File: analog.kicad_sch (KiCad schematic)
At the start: 0 parts

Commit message: Add analog schematic and refine wiring on top.
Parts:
- added C16: 100nF, Capacitor_SMD:C_0603_1608Metric_Pad1.08x0.95mm_HandSolder, symbol Device:C
- added D1, D2: BZT52H-AD3V3-QX, Diode_SMD:D_SOD-123F, symbol Diode:BZT52Bxx
- added R29: 0R, Resistor_SMD:R_0603_1608Metric_Pad0.98x0.95mm_HandSolder, symbol Device:R
- added R30: 15K, Resistor_SMD:R_0603_1608Metric_Pad0.98x0.95mm_HandSolder, symbol Device:R
- added R31: 10K, Resistor_SMD:R_0603_1608Metric_Pad0.98x0.95mm_HandSolder, symbol Device:R
- added R32: 4.7K, Resistor_SMD:R_0603_1608Metric_Pad0.98x0.95mm_HandSolder, symbol Device:R
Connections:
- new net: D1.1 (K), R29.1, R30.2, R31.2
- new net GNDA: C16.1, D1.2 (A), D2.2 (A), R30.1
- new net Van: R32.2
- new net moistv_mcu: C16.2, R31.1
- new net moistv_sensor: R29.2
- new net onewire_mcu: D2.1 (K), R32.1
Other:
- note added: "fc=0.1592KHz"

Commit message: Add protected Vbat charger input.
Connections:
- net GNDA renamed GNDD

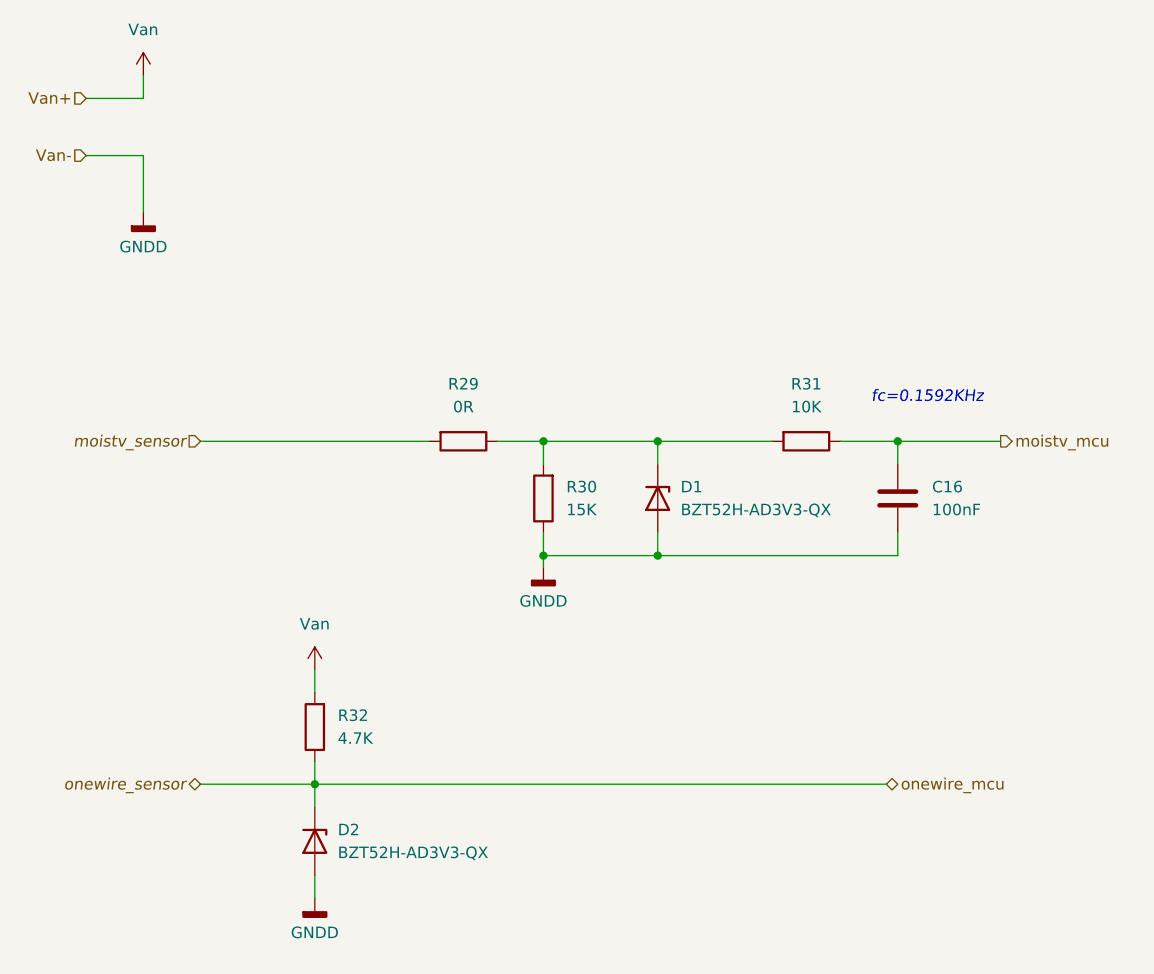
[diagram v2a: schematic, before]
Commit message: Add wiring, change footprint to avoid fatal errors at pads.
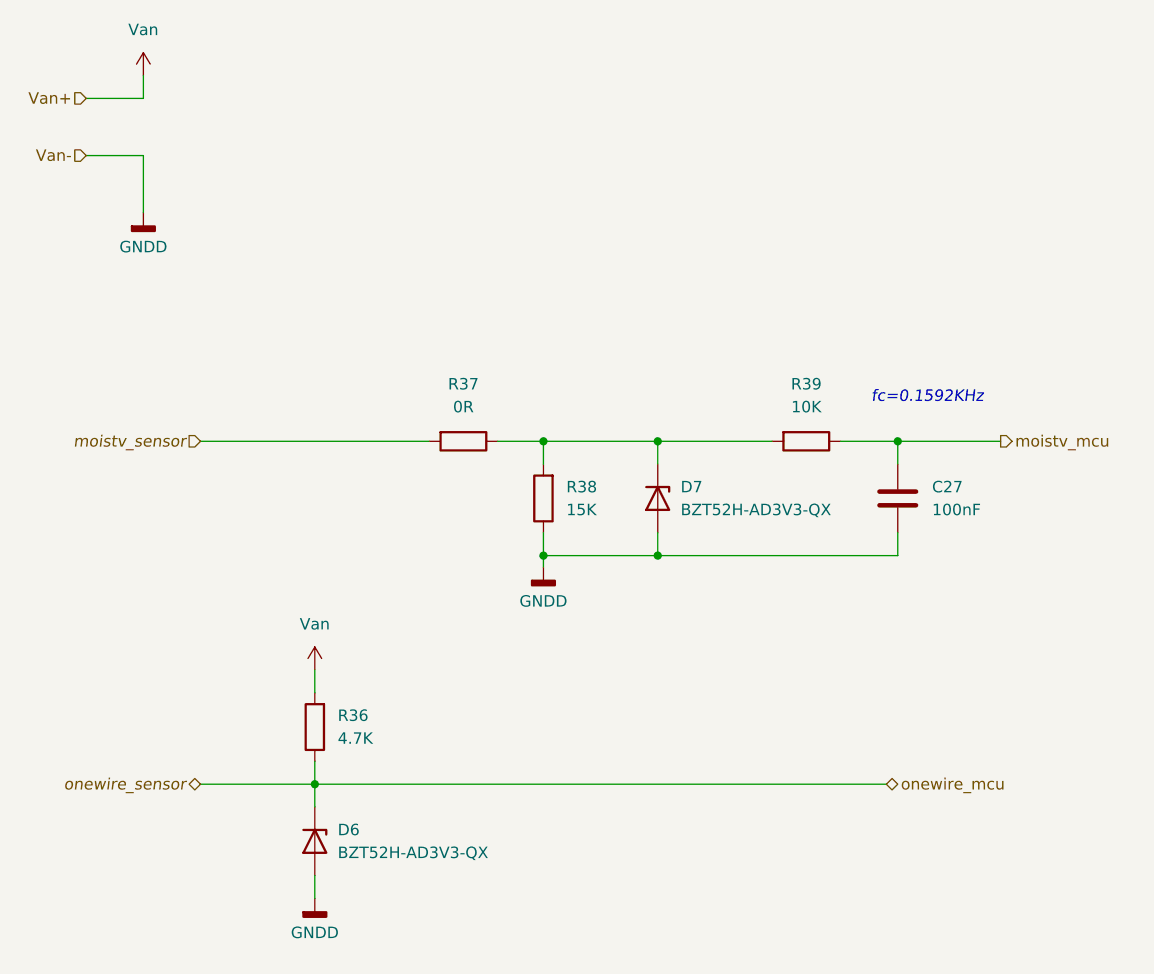
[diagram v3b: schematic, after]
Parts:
- renumbered C16 to C27, D2 to D6, D1 to D7, R32 to R36, R29 to R37, R30 to R38, R31 to R39
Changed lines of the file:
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@@
 		(dnp no)
 		(fields_autoplaced yes)
-		(property "Reference" "#PWR028"
+		(property "Reference" "#PWR068"
 			(at 50.8 120.65 0)
 			(hide yes)
@@
 			(project "MoistureESP"
 				(path "/f2b9f638-139e-46ec-aa60-77c4af989196/960f112a-382b-4f5d-84d2-6a2d0e442557"
-					(reference "#PWR028")
+					(reference "#PWR068")
 					(unit 1)
 				)
@@
 		(dnp no)
 		(fields_autoplaced yes)
-		(property "Reference" "R29"
+		(property "Reference" "R37"
 			(at 67.31 57.15 90)
 			(show_name no)
@@
 			(project "MoistureESP"
 				(path "/f2b9f638-139e-46ec-aa60-77c4af989196/960f112a-382b-4f5d-84d2-6a2d0e442557"
-					(reference "R29")
+					(reference "R37")
 					(unit 1)
 				)
@@
 		(dnp no)
 		(fields_autoplaced yes)
-		(property "Reference" "#PWR042"
+		(property "Reference" "#PWR067"
 			(at 50.8 92.71 0)
 			(hide yes)
@@
 			(project "MoistureESP"
 				(path "/f2b9f638-139e-46ec-aa60-77c4af989196/960f112a-382b-4f5d-84d2-6a2d0e442557"
-					(reference "#PWR042")
+					(reference "#PWR067")
 					(unit 1)
 				)
@@
 		(dnp no)
 		(fields_autoplaced yes)
-		(property "Reference" "D1"
+		(property "Reference" "D7"
 			(at 91.44 68.5799 90)
 			(show_name no)
@@
 			(project "MoistureESP"
 				(path "/f2b9f638-139e-46ec-aa60-77c4af989196/960f112a-382b-4f5d-84d2-6a2d0e442557"
-					(reference "D1")
+					(reference "D7")
 					(unit 1)
 				)
@@
 		(dnp no)
 		(fields_autoplaced yes)
-		(property "Reference" "#PWR033"
+		(property "Reference" "#PWR065"
 			(at 31.75 26.67 0)
 			(hide yes)
@@
 			(project "MoistureESP"
 				(path "/f2b9f638-139e-46ec-aa60-77c4af989196/960f112a-382b-4f5d-84d2-6a2d0e442557"
-					(reference "#PWR033")
+					(reference "#PWR065")
 					(unit 1)
 				)
@@
 		(dnp no)
 		(fields_autoplaced yes)
-		(property "Reference" "D2"
+		(property "Reference" "D6"
 			(at 53.34 106.6799 90)
 			(show_name no)
@@
 			(project "MoistureESP"
 				(path "/f2b9f638-139e-46ec-aa60-77c4af989196/960f112a-382b-4f5d-84d2-6a2d0e442557"
-					(reference "D2")
+					(reference "D6")
 					(unit 1)
 				)
@@
 		(dnp no)
 		(fields_autoplaced yes)
-		(property "Reference" "R32"
+		(property "Reference" "R36"
 			(at 53.34 93.9799 0)
 			(show_name no)
@@
 			(project "MoistureESP"
 				(path "/f2b9f638-139e-46ec-aa60-77c4af989196/960f112a-382b-4f5d-84d2-6a2d0e442557"
-					(reference "R32")
+					(reference "R36")
 					(unit 1)
 				)
@@
 		(dnp no)
 		(fields_autoplaced yes)
-		(property "Reference" "#PWR030"
+		(property "Reference" "#PWR066"
 			(at 31.75 44.45 0)
 			(hide yes)
@@
 			(project "MoistureESP"
 				(path "/f2b9f638-139e-46ec-aa60-77c4af989196/960f112a-382b-4f5d-84d2-6a2d0e442557"
-					(reference "#PWR030")
+					(reference "#PWR066")
 					(unit 1)
 				)
@@
 		(dnp no)
 		(fields_autoplaced yes)
-		(property "Reference" "R31"
+		(property "Reference" "R39"
 			(at 105.41 57.15 90)
 			(show_name no)
@@
 			(project "MoistureESP"
 				(path "/f2b9f638-139e-46ec-aa60-77c4af989196/960f112a-382b-4f5d-84d2-6a2d0e442557"
-					(reference "R31")
+					(reference "R39")
 					(unit 1)
 				)
@@
 		(dnp no)
 		(fields_autoplaced yes)
-		(property "Reference" "#PWR027"
+		(property "Reference" "#PWR069"
 			(at 76.2 83.82 0)
 			(hide yes)
@@
 			(project "MoistureESP"
 				(path "/f2b9f638-139e-46ec-aa60-77c4af989196/960f112a-382b-4f5d-84d2-6a2d0e442557"
-					(reference "#PWR027")
+					(reference "#PWR069")
 					(unit 1)
 				)
@@
 		(dnp no)
 		(fields_autoplaced yes)
-		(property "Reference" "R30"
+		(property "Reference" "R38"
 			(at 78.74 68.5799 0)
 			(show_name no)
@@
 			(project "MoistureESP"
 				(path "/f2b9f638-139e-46ec-aa60-77c4af989196/960f112a-382b-4f5d-84d2-6a2d0e442557"
-					(reference "R30")
+					(reference "R38")
 					(unit 1)
 				)
@@
 		(dnp no)
 		(fields_autoplaced yes)
-		(property "Reference" "C16"
+		(property "Reference" "C27"
 			(at 119.38 68.5799 0)
 			(show_name no)
@@
 			(project "MoistureESP"
 				(path "/f2b9f638-139e-46ec-aa60-77c4af989196/960f112a-382b-4f5d-84d2-6a2d0e442557"
-					(reference "C16")
-					(unit 1)
-				)
+					(reference "C27")
+					(unit 1)
+				)

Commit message: Export BOM, change page headers.
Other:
- company: (none) -> B.Major
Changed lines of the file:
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@@
 	(generator_version "10.0")
 	(paper "A4")
+	(title_block
+		(date "2026-03-27")
+		(rev "1")
+		(company "B.Major")
+	)
 	(text "fc=0.1592KHz"
 		(exclude_from_sim no)
